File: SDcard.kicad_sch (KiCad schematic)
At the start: 4 parts, among them J17 Micro_SD_Card_Det1

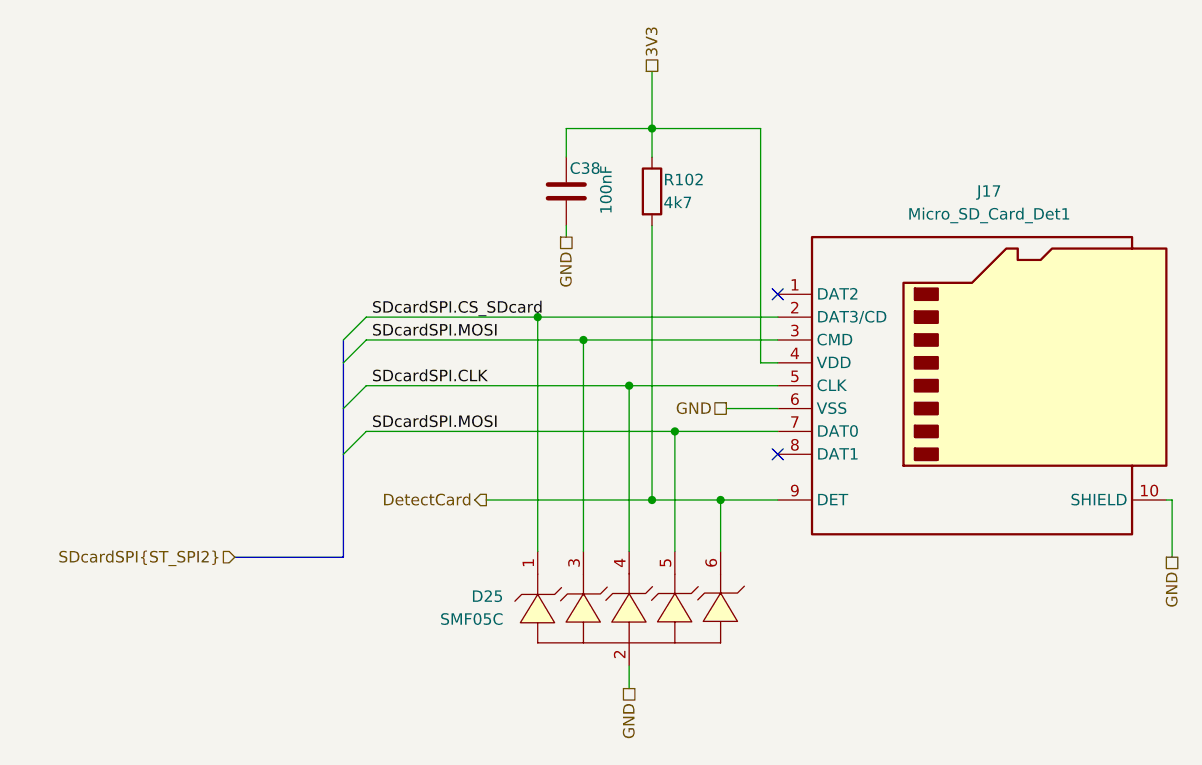
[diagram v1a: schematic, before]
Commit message: Layout p2, fix Analog VCC and GND for opamp circuit
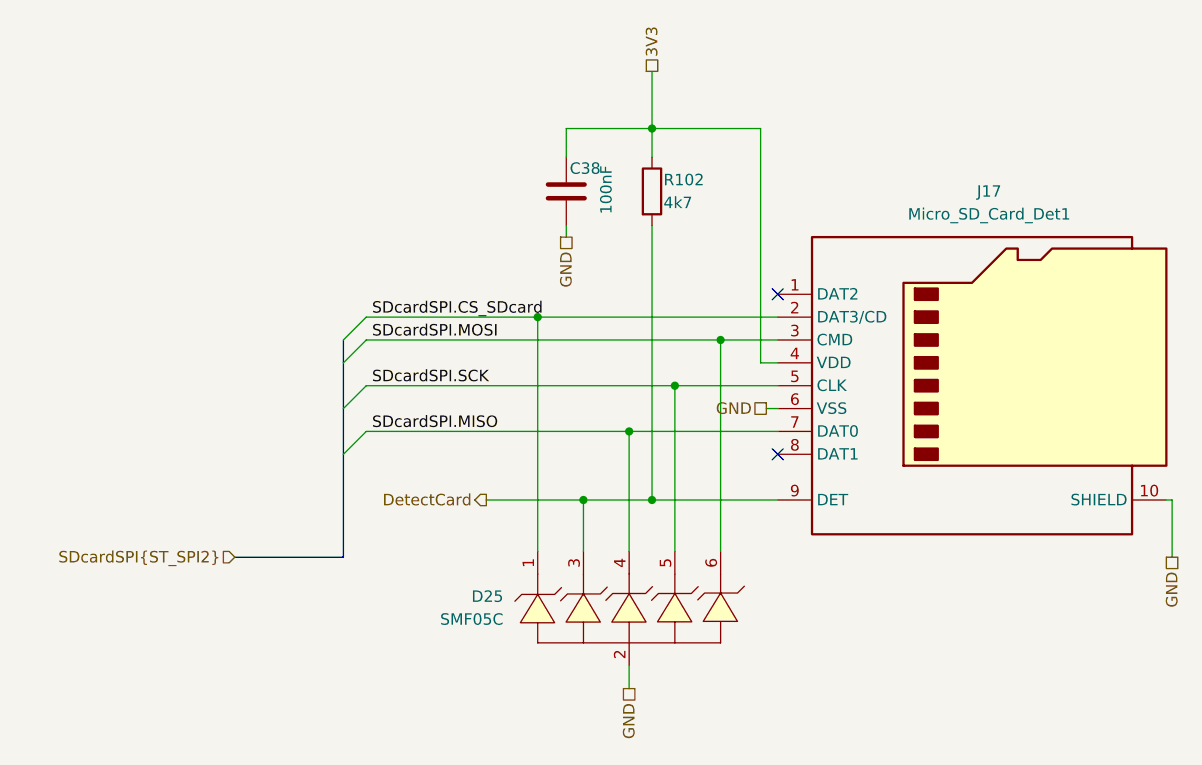
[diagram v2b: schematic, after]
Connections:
- net DetectCard: now also D25.3; no longer D25.6
- net SDcardSPI.MOSI: now also D25.6; no longer D25.3, D25.5, J17.7 (DAT0)
- net SDcardSPI.CLK renamed SDcardSPI.MISO
- net SDcardSPI.MISO: now also J17.7 (DAT0); no longer J17.5 (CLK)
- new net SDcardSPI.SCK: D25.5, J17.5 (CLK)
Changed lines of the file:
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@@
 	(paper "A4")
 	(junction
-		(at 104.14 85.09)
-		(diameter 0)
-		(color 0 0 0 0)
-	)
-	(junction
-		(at 109.22 90.17)
-		(diameter 0)
-		(color 0 0 0 0)
-	)
-	(junction
-		(at 99.06 80.01)
+		(at 114.3 80.01)
+		(diameter 0)
+		(color 0 0 0 0)
+	)
+	(junction
+		(at 99.06 97.79)
+		(diameter 0)
+		(color 0 0 0 0)
+	)
+	(junction
+		(at 104.14 90.17)
 		(diameter 0)
 		(color 0 0 0 0)
@@
 	)
 	(junction
-		(at 114.3 97.79)
+		(at 109.22 85.09)
 		(diameter 0)
 		(color 0 0 0 0)
@@
 	(wire
 		(pts
-			(xy 74.93 85.09) (xy 104.14 85.09)
+			(xy 104.14 90.17) (xy 104.14 103.505)
 		)
 		(stroke
@@
 	(wire
 		(pts
-			(xy 114.3 97.79) (xy 114.3 103.505)
+			(xy 99.06 97.79) (xy 106.68 97.79)
 		)
 		(stroke
@@
 	(wire
 		(pts
-			(xy 109.22 90.17) (xy 120.65 90.17)
+			(xy 74.93 90.17) (xy 104.14 90.17)
 		)
 		(stroke
@@
 	(wire
 		(pts
-			(xy 104.14 85.09) (xy 120.65 85.09)
+			(xy 74.93 85.09) (xy 109.22 85.09)
 		)
 		(stroke
@@
 	(wire
 		(pts
-			(xy 114.935 87.63) (xy 120.65 87.63)
+			(xy 119.38 87.63) (xy 120.65 87.63)
+		)
+		(stroke
+			(width 0)
+			(type default)
+		)
+	)
+	(wire
+		(pts
+			(xy 109.22 85.09) (xy 120.65 85.09)
 		)
 		(stroke
@@
 	(wire
 		(pts
-			(xy 99.06 80.01) (xy 99.06 103.505)
+			(xy 109.22 85.09) (xy 109.22 103.505)
 		)
 		(stroke
@@
 	(wire
 		(pts
-			(xy 99.06 80.01) (xy 120.65 80.01)
+			(xy 99.06 97.79) (xy 99.06 103.505)
 		)
 		(stroke
@@
 		)
 	)
+	(wire
+		(pts
+			(xy 114.3 80.01) (xy 120.65 80.01)
+		)
+		(stroke
+			(width 0)
+			(type default)
+		)
+	)
 	(bus
 		(pts
@@
 	(wire
 		(pts
-			(xy 109.22 90.17) (xy 109.22 103.505)
+			(xy 104.14 90.17) (xy 120.65 90.17)
 		)
 		(stroke
@@
 	(wire
 		(pts
-			(xy 114.3 97.79) (xy 120.65 97.79)
-		)
-		(stroke
-			(width 0)
-			(type default)
-		)
-	)
-	(wire
-		(pts
-			(xy 74.93 80.01) (xy 99.06 80.01)
+			(xy 106.68 97.79) (xy 120.65 97.79)
+		)
+		(stroke
+			(width 0)
+			(type default)
+		)
+	)
+	(wire
+		(pts
+			(xy 74.93 80.01) (xy 114.3 80.01)
 		)
 		(stroke
@@
 	(wire
 		(pts
-			(xy 106.68 97.79) (xy 114.3 97.79)
+			(xy 114.3 80.01) (xy 114.3 103.505)
 		)
 		(stroke
@@
 	(wire
 		(pts
-			(xy 88.265 97.79) (xy 106.68 97.79)
-		)
-		(stroke
-			(width 0)
-			(type default)
-		)
-	)
-	(wire
-		(pts
-			(xy 74.93 90.17) (xy 109.22 90.17)
-		)
-		(stroke
-			(width 0)
-			(type default)
-		)
-	)
-	(wire
-		(pts
-			(xy 104.14 85.09) (xy 104.14 103.505)
-		)
-		(stroke
-			(width 0)
-			(type default)
-		)
-	)
-	(label "SDcardSPI.MOSI"
+			(xy 88.265 97.79) (xy 99.06 97.79)
+		)
+		(stroke
+			(width 0)
+			(type default)
+		)
+	)
+	(label "SDcardSPI.MISO"
 		(at 75.565 90.17 0)
 		(fields_autoplaced yes)
@@
 		)
 	)
-	(label "SDcardSPI.CLK"
+	(label "SDcardSPI.SCK"
 		(at 75.565 85.09 0)
 		(fields_autoplaced yes)
@@
 	(hierarchical_label "GND"
 		(shape passive)
-		(at 114.935 87.63 180)
-		(fields_autoplaced yes)
-		(effects
+		(at 119.38 87.63 180)
+		(fields_autoplaced yes)
+		(effects
